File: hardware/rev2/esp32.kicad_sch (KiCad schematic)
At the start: 38 parts, among them J6 uFL, SW1 SW_Push, SW2 SW_Push, U2 ESP32-S3FN8, Y1 ECS-2520SMV-400-FN-TR

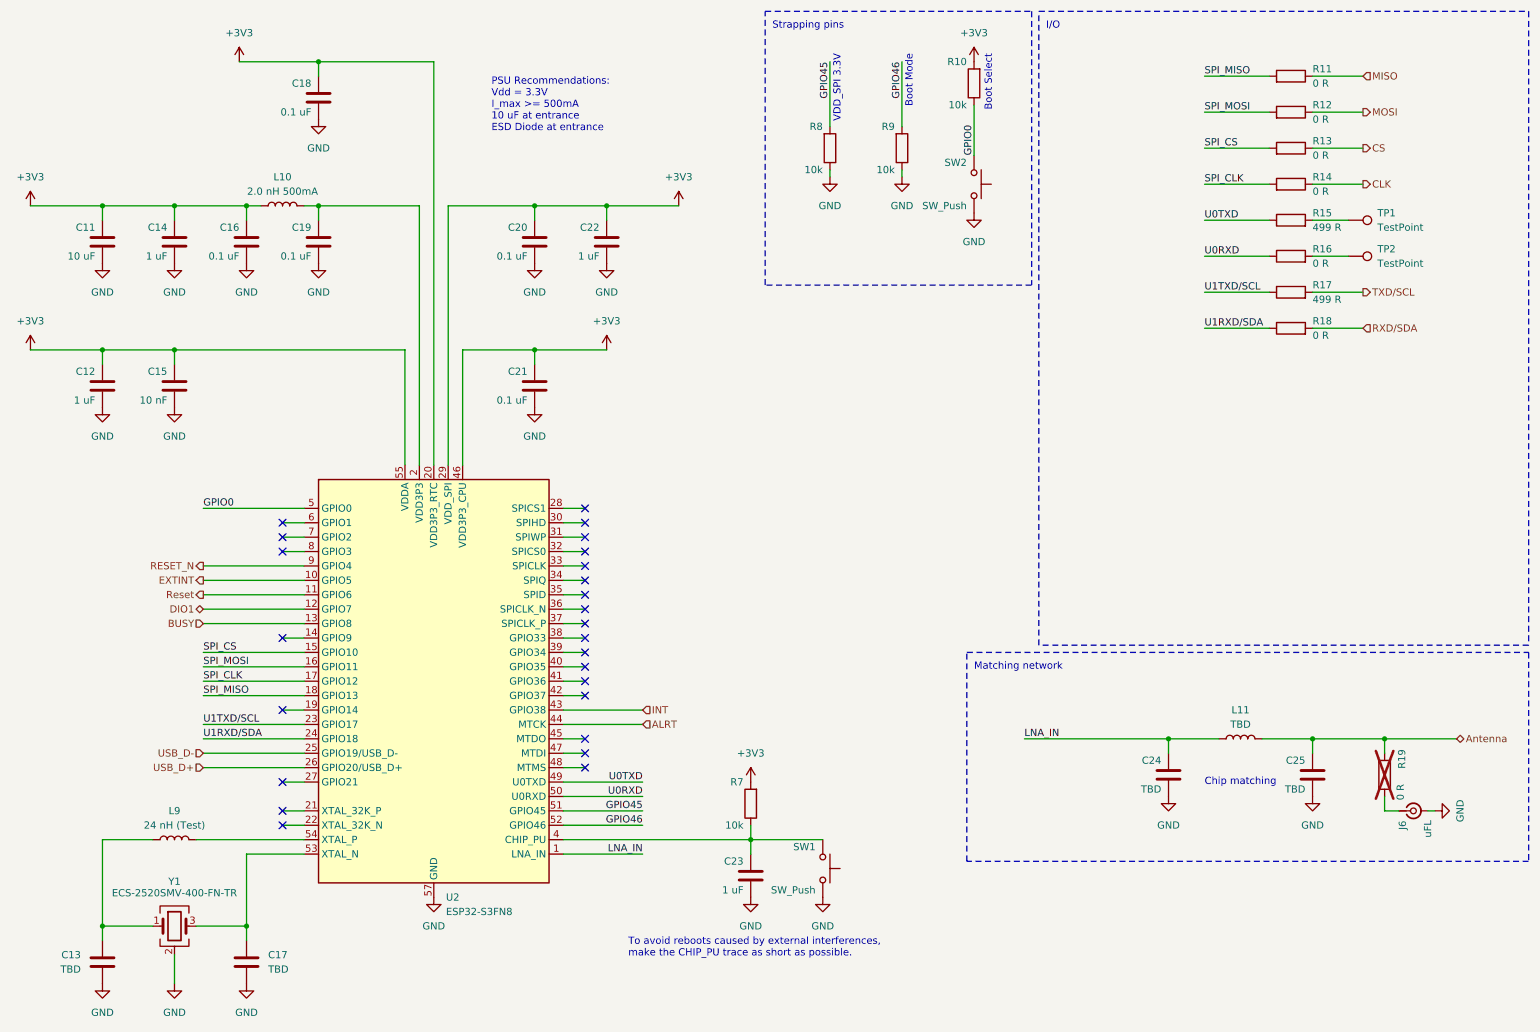
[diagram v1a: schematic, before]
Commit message: added testpoints, added LEDs, fixed a lot of DRC stuff
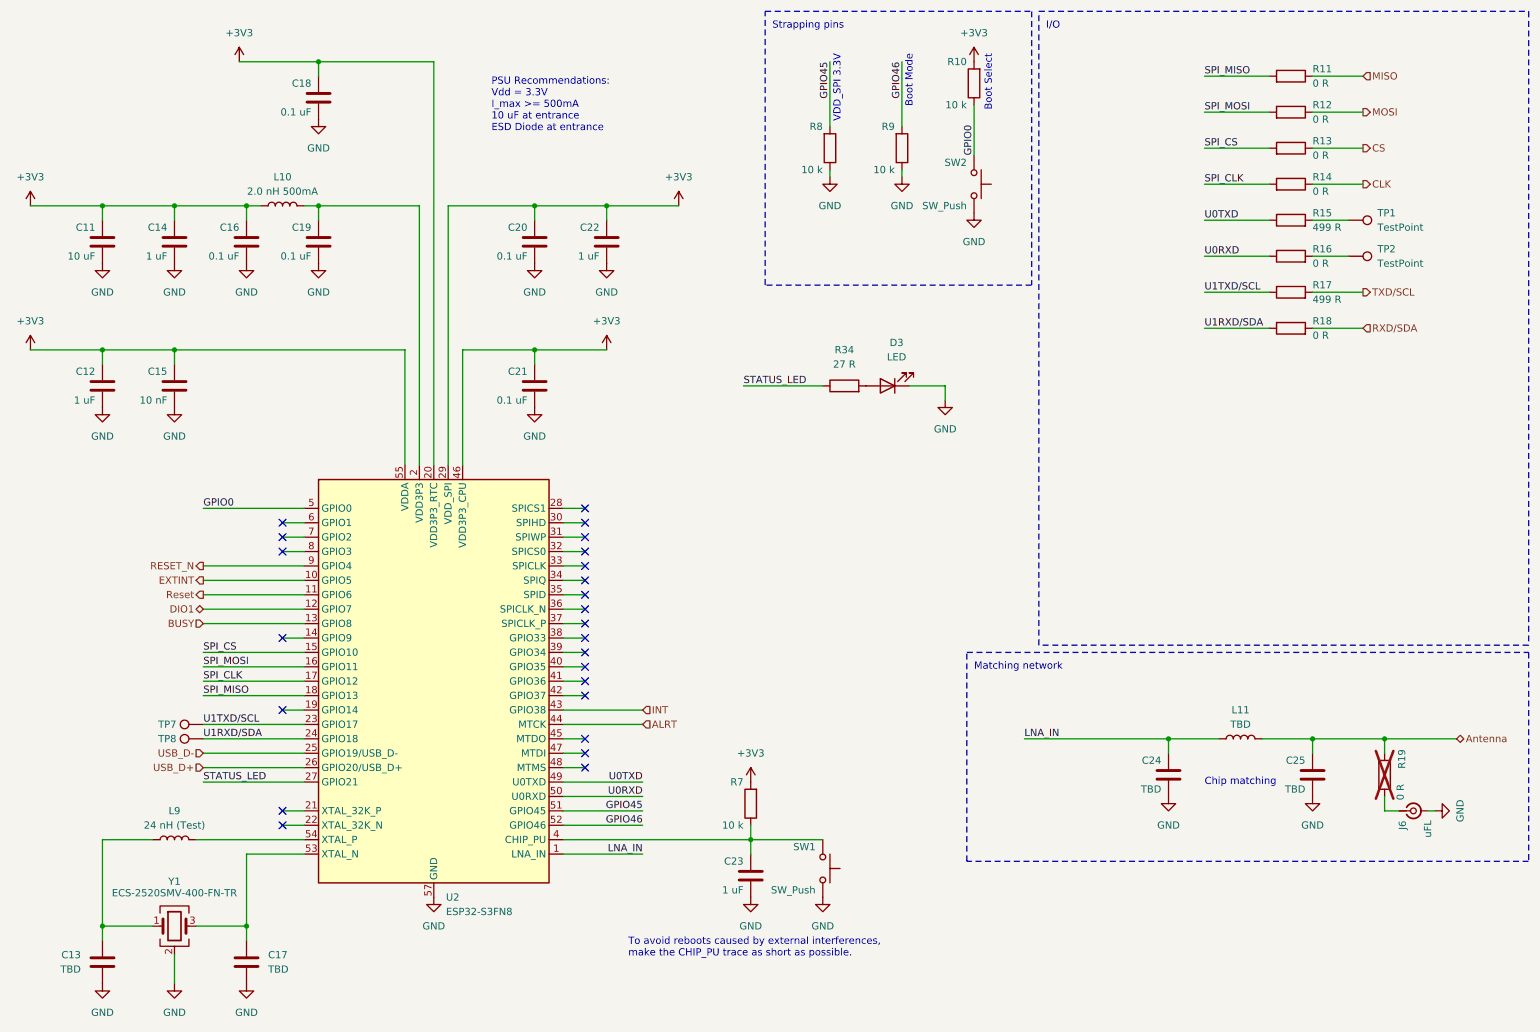
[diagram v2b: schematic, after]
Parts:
- added D3: LED, LED_SMD:LED_0603_1608Metric_Pad1.05x0.95mm_HandSolder, symbol Device:LED
- added R34: 27 R, Resistor_SMD:R_0603_1608Metric_Pad0.98x0.95mm_HandSolder, symbol Device:R
- added TP7, TP8: TestPoint, TestPoint:TestPoint_Pad_D1.0mm, symbol Connector:TestPoint
- C12, C14, C22, C23: Mouser Part Number (none) -> 81-GRM188R61C105KA2J
- L10: footprint Inductor_SMD:L_0603_1608Metric_Pad1.05x0.95mm_HandSolder -> Inductor_SMD:L_0402_1005Metric_Pad0.77x0.64mm_HandSolder; Mouser Part Number (none) -> 279-36550402S2N0T
- L9: Mouser Part Number (none) -> 81-LQP03TN24NH02D
- R10, R7, R8, R9: value 10k -> 10 k; footprint Inductor_SMD:L_0603_1608Metric_Pad1.05x0.95mm_HandSolder -> Resistor_SMD:R_0603_1608Metric_Pad0.98x0.95mm_HandSolder; Mouser Part Number (none) -> 71-CRCW060310K0JNEAC
- R15, R17: footprint Inductor_SMD:L_0603_1608Metric_Pad1.05x0.95mm_HandSolder -> Resistor_SMD:R_0603_1608Metric_Pad0.98x0.95mm_HandSolder; Mouser Part Number (none) -> 71-CRCW0603499RFKEAC
- R19: Mouser Part Number 71-CRCW04020000Z0EDC -> 71-CRCW04020000Z0EDC
- U2: Mouser Part Number (none) -> 356-ESP32-S3FN8
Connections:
- net GND: now also D3.1 (K)
- net U1RXD/SDA: now also TP8.1
- net U1TXD/SCL: now also TP7.1
- net STATUS_LED: now reaches U2.27 (GPIO21)
- net STATUS_LED: now also R34.1
- new net: D3.2 (A), R34.2
- no-connect marks 25 -> 24

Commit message: changed layout a bit, updated footprints, did stuff
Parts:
- R17: value 499 R -> 0 R
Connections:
- net U1RXD/SDA is gone; now on net SDA: R18.1, TP8.1, U2.24 (GPIO18)
- net U1TXD/SCL is gone; now on net SCL: R17.1, TP7.1, U2.23 (GPIO17)
- net RXD/SDA renamed SDA
- net TXD/SCL renamed SCL
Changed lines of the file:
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@@
 		)
 	)
-	(label "U1RXD{slash}SDA"
+	(label "SDA"
 		(at 226.06 69.85 0)
 		(effects
@@
 		)
 	)
-	(label "U1TXD{slash}SCL"
+	(label "SCL"
 		(at 49.53 139.7 0)
 		(effects
@@
 		)
 	)
-	(label "U1TXD{slash}SCL"
+	(label "SCL"
 		(at 226.06 63.5 0)
 		(effects
@@
 		)
 	)
-	(label "U1RXD{slash}SDA"
+	(label "SDA"
 		(at 49.53 142.24 0)
 		(effects
@@
 		)
 	)
-	(hierarchical_label "RXD{slash}SDA"
+	(hierarchical_label "SDA"
 		(shape input)
 		(at 254 69.85 0)
@@
 		)
 	)
-	(hierarchical_label "TXD{slash}SCL"
+	(hierarchical_label "SCL"
 		(shape output)
 		(at 254 63.5 0)
@@
 			)
 		)
-		(property "Value" "499 R"
+		(property "Value" "0 R"
 			(at 245.11 64.77 90)
 			(show_name no)

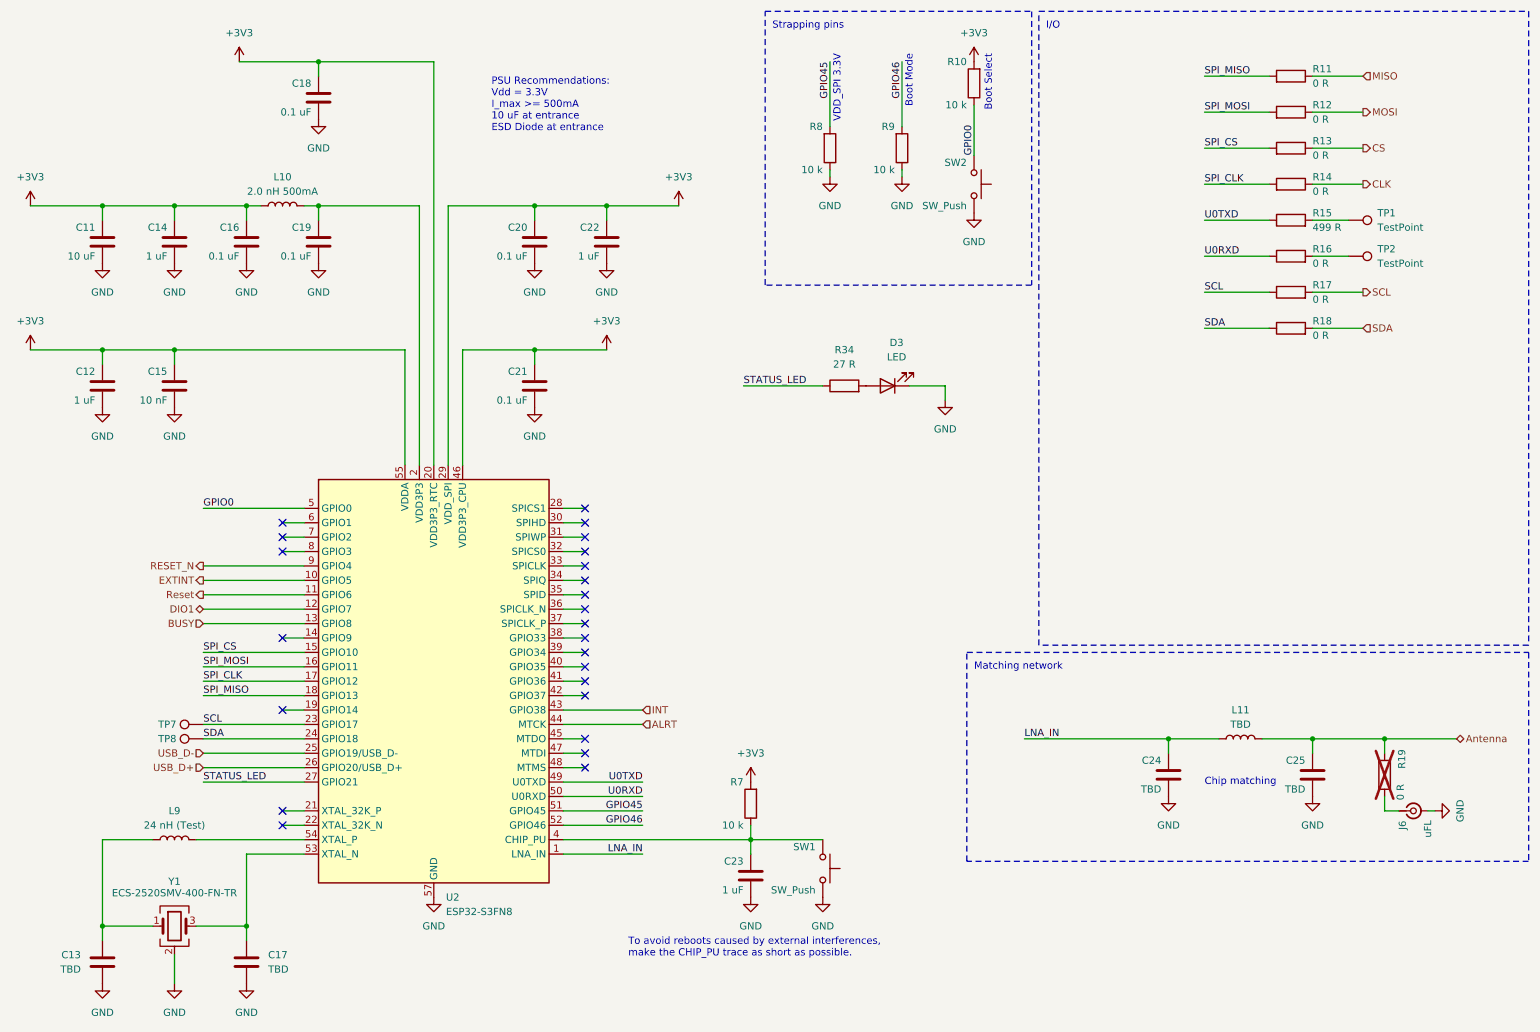
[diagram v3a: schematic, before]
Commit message: finished PCB v1, changed rf connector layout, added vias, added footprints for RF filtering
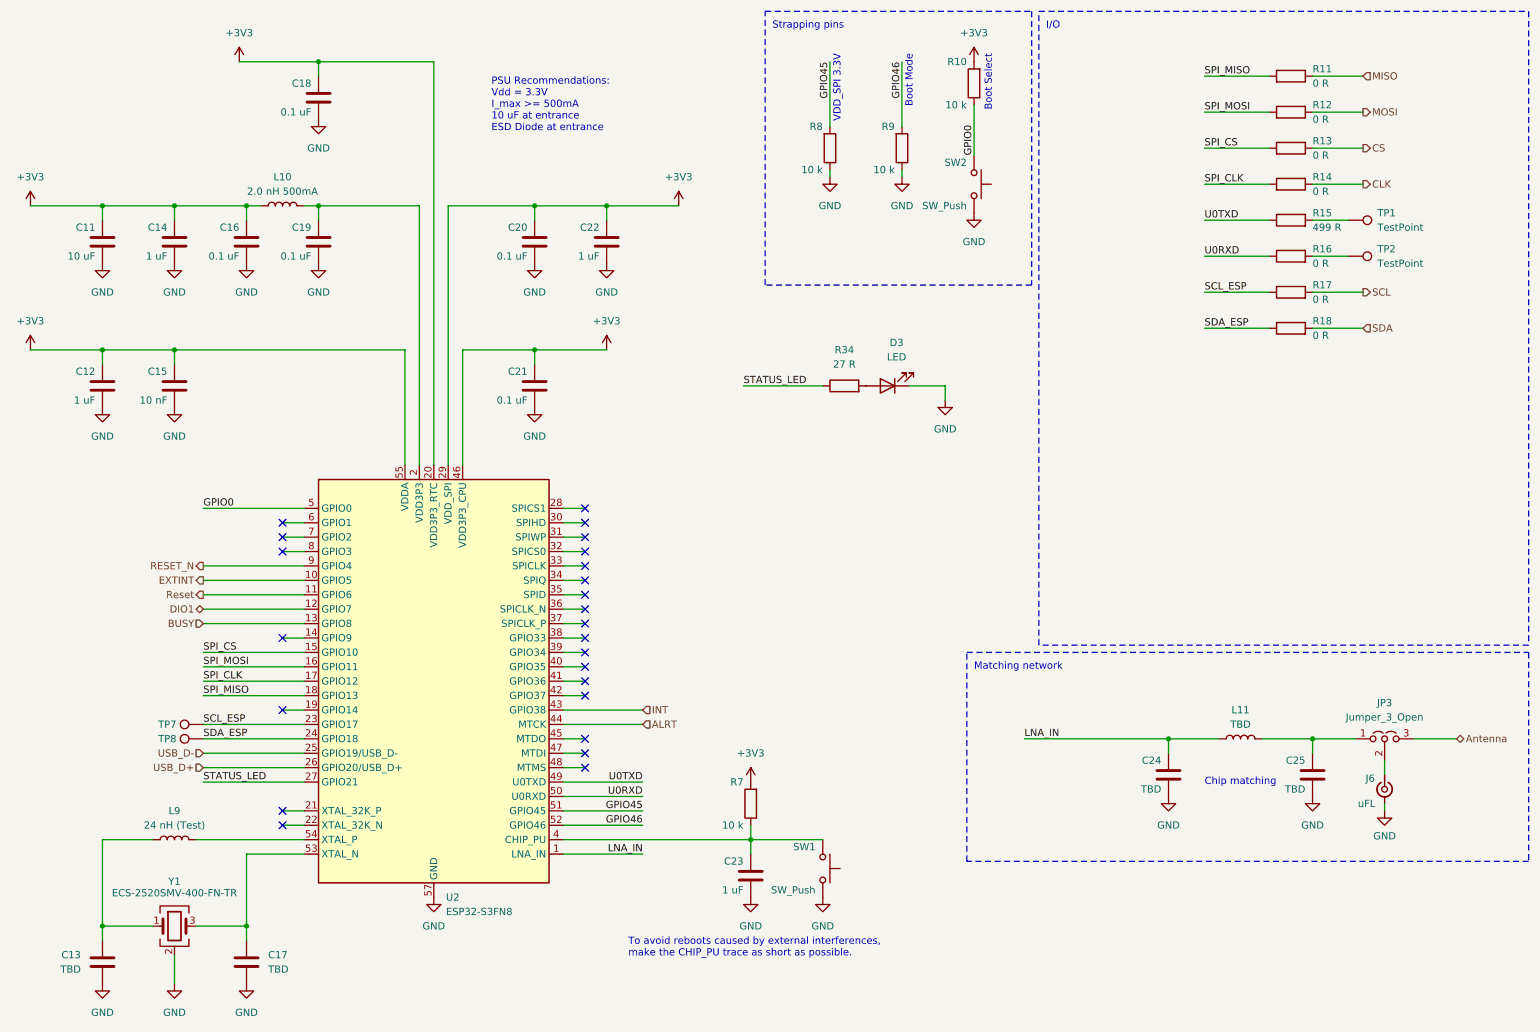
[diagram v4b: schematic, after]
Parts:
- removed R19: 0 R, Resistor_SMD:R_0402_1005Metric_Pad0.72x0.64mm_HandSolder, symbol Device:R
- added JP3: Jumper_3_Open, _footprints:Jumper_3_R_0402_1005Metric_Pad0.72x0.64mm_HandSolder, symbol Jumper:Jumper_3_Open
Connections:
- net Antenna: now also JP3.3 (B); no longer C25.1, L11.1
- net SCL: no longer R17.1, TP7.1, U2.23 (GPIO17)
- net SDA: no longer R18.1, TP8.1, U2.24 (GPIO18)
- net at J6.1 (In): now also JP3.2 (C)
- new net: C25.1, JP3.1 (A), L11.1
- new net SCL_ESP: R17.1, TP7.1, U2.23 (GPIO17)
- new net SDA_ESP: R18.1, TP8.1, U2.24 (GPIO18)
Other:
- moved on the sheet: J6

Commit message: fixed soldermask and silkscreen mostly
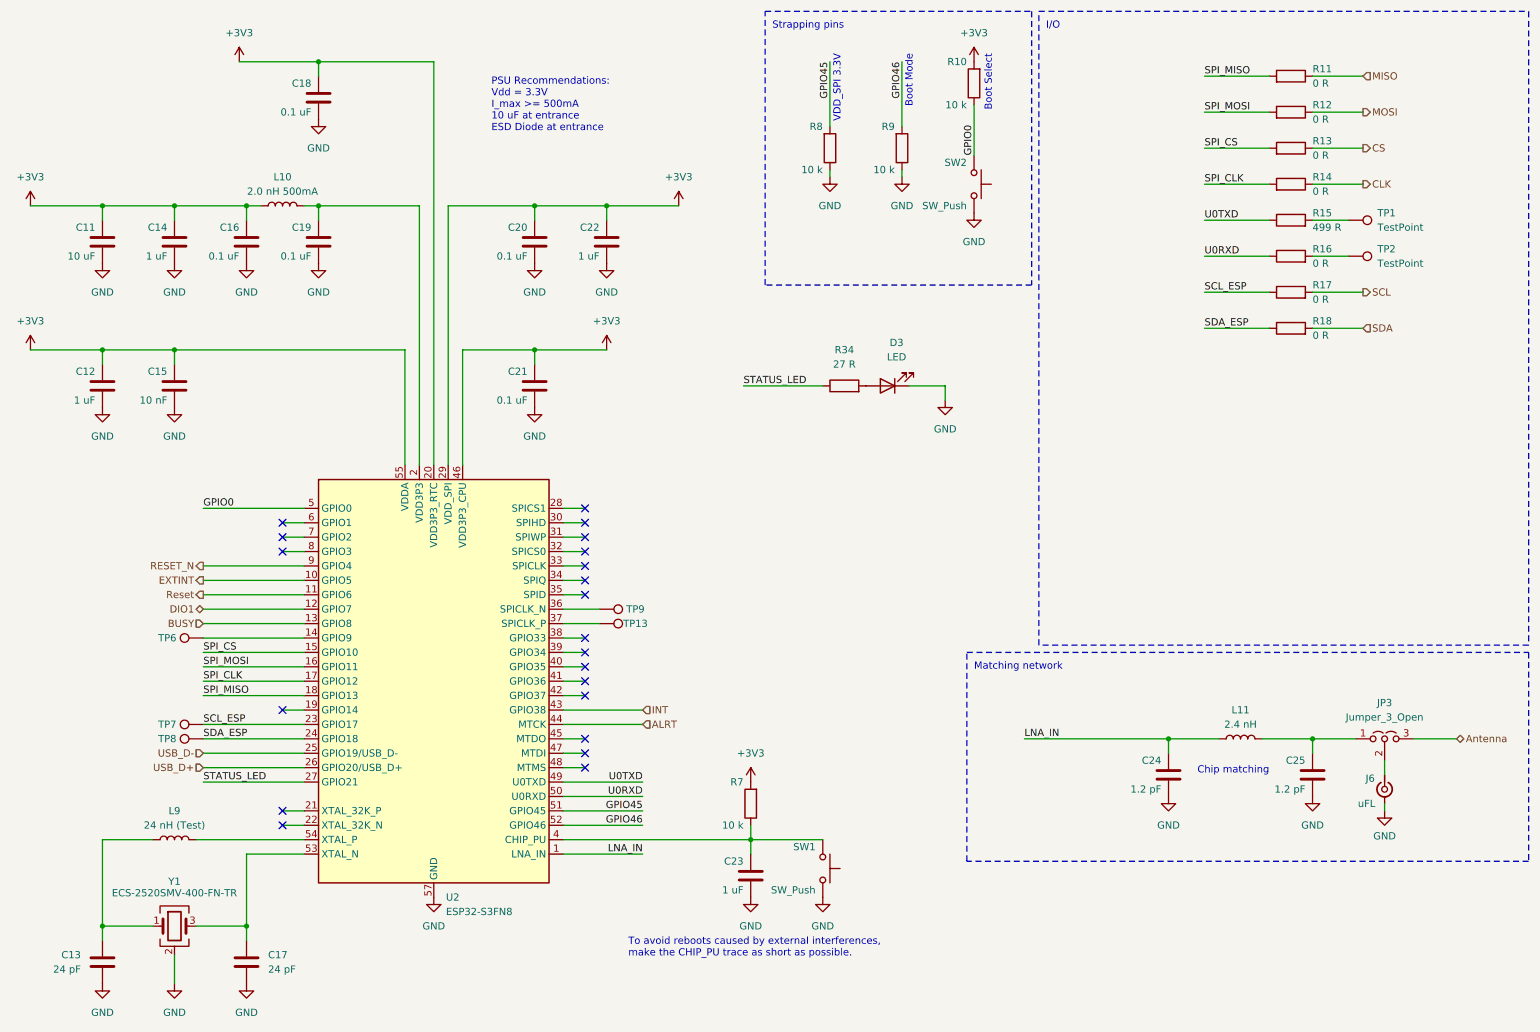
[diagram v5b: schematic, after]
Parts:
- added TP13, TP6, TP9: TestPoint, TestPoint:TestPoint_Pad_D1.0mm, symbol Connector:TestPoint
- C13, C17: value TBD -> 24 pF; Mouser Part Number (none) -> 81-GCM1885C2A240JA6D
- C24, C25: value TBD -> 1.2 pF; Mouser Part Number (none) -> 81-GRM1555C1H1R2CA1J
- JP3: Mouser Part Number (none) -> 71-CRCW04020000Z0EDC; now in the parts list
- L11: value TBD -> 2.4 nH; Mouser Part Number (none) -> 81-LQG15HN2N4S02D
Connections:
- net at U2.14 (GPIO9): now also TP6.1
- net at U2.36 (SPICLK_N): now also TP9.1
- net at U2.37 (SPICLK_P): now also TP13.1
- no-connect marks 24 -> 21

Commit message: final edit, send to production
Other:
- company: MMCX11 -> Group 10
- title: ESP32 -> LoRa Based Cat Tracker
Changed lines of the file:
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@@
 	(paper "A4")
 	(title_block
-		(title "ESP32")
-		(date "2026-03-31")
-		(rev "1")
-		(company "MMCX11")
+		(title "LoRa Based Cat Tracker")
+		(date "2026-04-22")
+		(rev "2.0.0")
+		(company "Group 10")
 	)
 	(rectangle

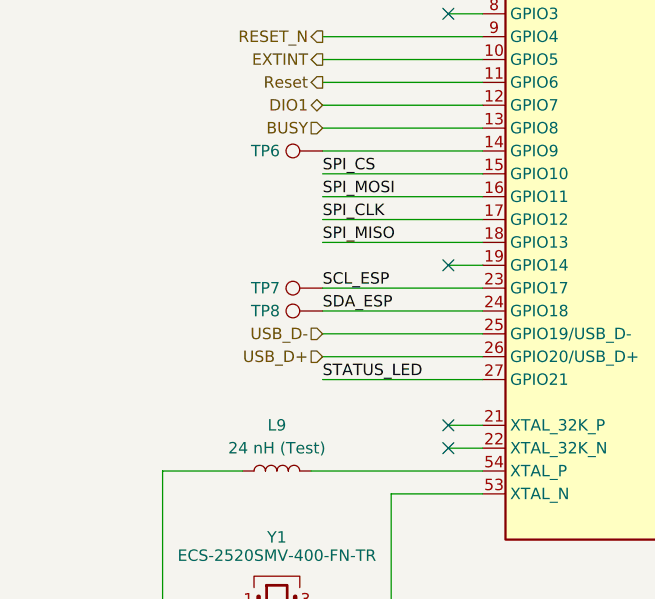
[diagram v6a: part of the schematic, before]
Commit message: added resistors
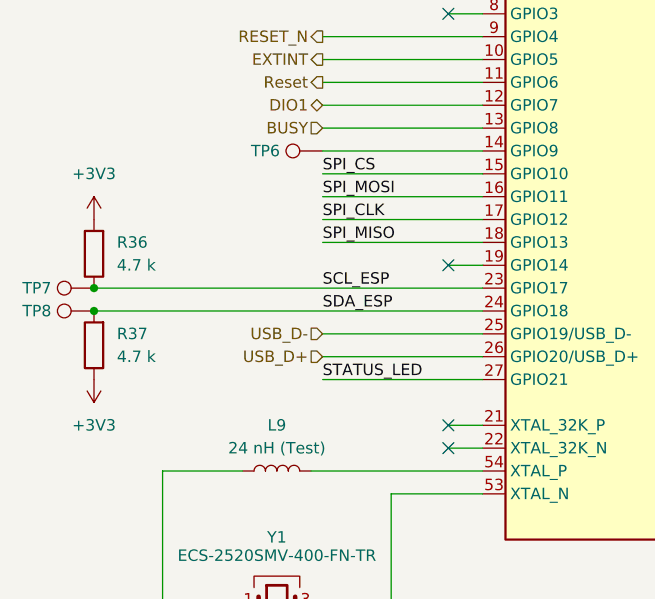
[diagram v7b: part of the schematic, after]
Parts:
- added R36, R37: 4.7 k, Resistor_SMD:R_0603_1608Metric_Pad0.98x0.95mm_HandSolder, symbol Device:R
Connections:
- net +3V3: now also R36.2, R37.1
- net SCL_ESP: now also R36.1
- net SDA_ESP: now also R37.2
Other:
- moved on the sheet: TP7, TP8
